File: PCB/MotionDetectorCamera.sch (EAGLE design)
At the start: 186 parts, among them J1 JUMPER-SOLDER, J10 MICROSD-SOCKET, J11 USB-C-JACK, J2 JUMPER-SOLDER, J3 JUMPER-SOLDER, J4 JUMPER-SOLDER, J5 JST-PH-2, J6 JUMPER-SOLDER, J7 JUMPER-SOLDER, J8 JUMPER-SOLDER, J9 S-MOUNT-LENS-HOLDER, Q1 PMOS-NEXPERIA-SOT1220, Q2 PMOS-NEXPERIA-SOT1220, Q3 PMOS-NEXPERIA-SOT1220, U1 TI-TPS2116, U10 TI-TPS22919DCK, U11 TI-TPS62A01, U13 TI-TPS22919DCK, U14 TI-TPS22919DCK, U15 TI-MSP430FR2422IRHL, U16 NXP-NTB0102, U17 NXP-NTB0102, U18 PANASONIC-EKMB110711X, U19 LATTICE-ICE40HX4K-BG121, U2 DIODESINC-AP7350, U20 WINBOND-W25Q40EW, U21 NEXPERIA-74LVC1G98-OR-INV-INP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, U22 NEXPERIA-74LVC1G98-BUFFER, U23 ON-AR0330CS1C12SPKA0, U24 ALLIANCE-AS4C8M16MSA-6BIN, U25 STM-STM32F730, U26 DIODESINC-DT1446-04V-7, U27 NEXPERIA-74LVC1G98-BUFFER, U3 NEXPERIA-74LVC1G98-NOR, U4 MICROCHIP-MCP7383X, U5 EATON-STN101, U6 TI-TPS62A01, U7 TI-TPS62A01, U9 TI-TPS22919DCK, X1 EPSON-FC-135, X2 SITIME-SIT8021, X3 SITIME-SIT8021

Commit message: Switch to smaller lens holder (PT-LH008P)
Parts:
- J9: value S-MOUNT-LENS-HOLDER -> S-MOUNT-LENS-HOLDERM12LENSES-PT-LH008P; device EagleLibrary:S-MOUNT-LENS-HOLDER -> EagleLibrary:S-MOUNT-LENS-HOLDERM12LENSES-PT-LH008P; MFG Marshall Electronics -> (none); PN V-LH4 -> (none)
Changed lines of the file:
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@@
 </part>
 <part name="TP2" library="EagleLibrary" deviceset="TEST-POINT" device=""/>
-<part name="J9" library="EagleLibrary" deviceset="S-MOUNT-LENS-HOLDER" device="">
-<attribute name="MFG" value="Marshall Electronics"/>
-<attribute name="PN" value="V-LH4"/>
-</part>
+<part name="J9" library="EagleLibrary" deviceset="S-MOUNT-LENS-HOLDER" device="M12LENSES-PT-LH008P"/>
 <part name="U25" library="EagleLibrary" deviceset="STM-STM32F730" device="">
 <attribute name="PN" value="STM32F730I8K6"/>

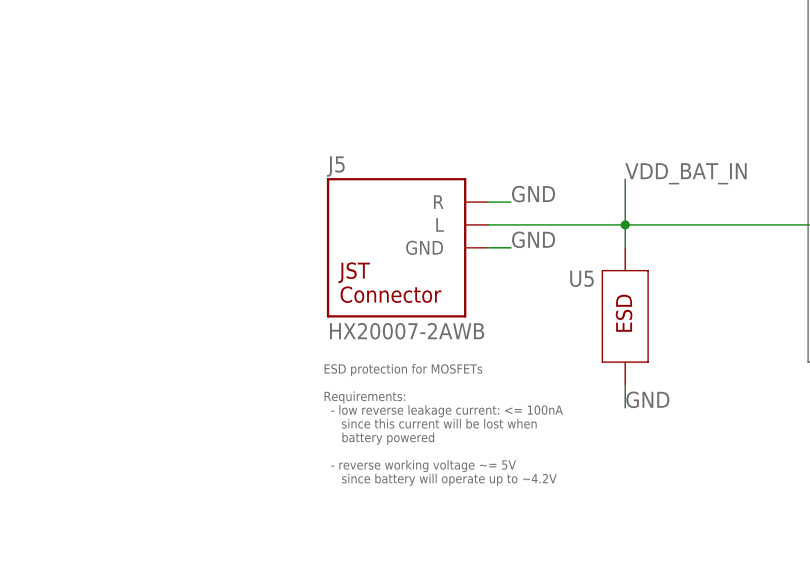
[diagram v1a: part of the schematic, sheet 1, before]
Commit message: Replace battery connector with a smaller version, and move it to the front of the board
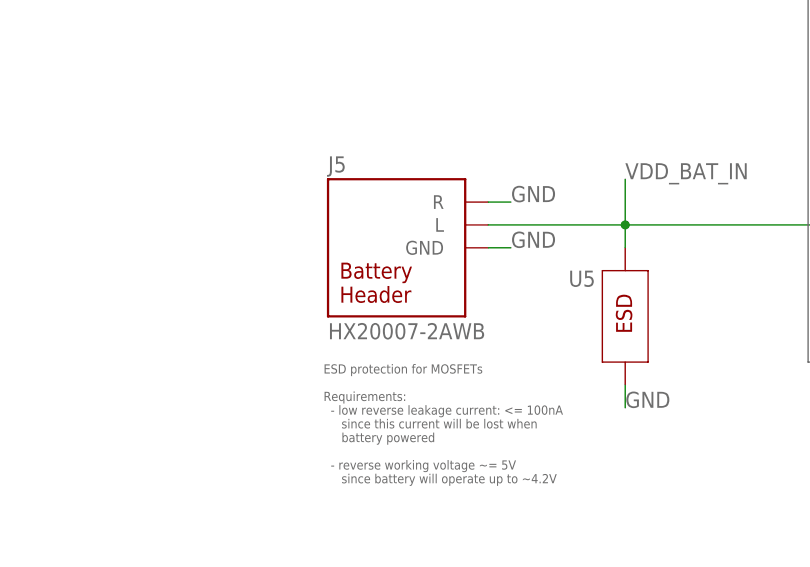
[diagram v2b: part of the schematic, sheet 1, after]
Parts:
- J5: value JST-PH-2 -> JST-SM02B-SRSS-TB; device EagleLibrary:JST-PH-2 -> EagleLibrary:JST-SM02B-SRSS-TB
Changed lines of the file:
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@@
 <attribute name="PN" value="STN101050B101"/>
 </part>
-<part name="J5" library="EagleLibrary" deviceset="JST-PH-2" device="">
+<part name="J5" library="EagleLibrary" deviceset="JST-SM02B-SRSS-TB" device="">
 <attribute name="MFG" value="HX (Zhejiang Yueqing Hongxing Elec)"/>
 <attribute name="MFG2" value="HDGC"/>

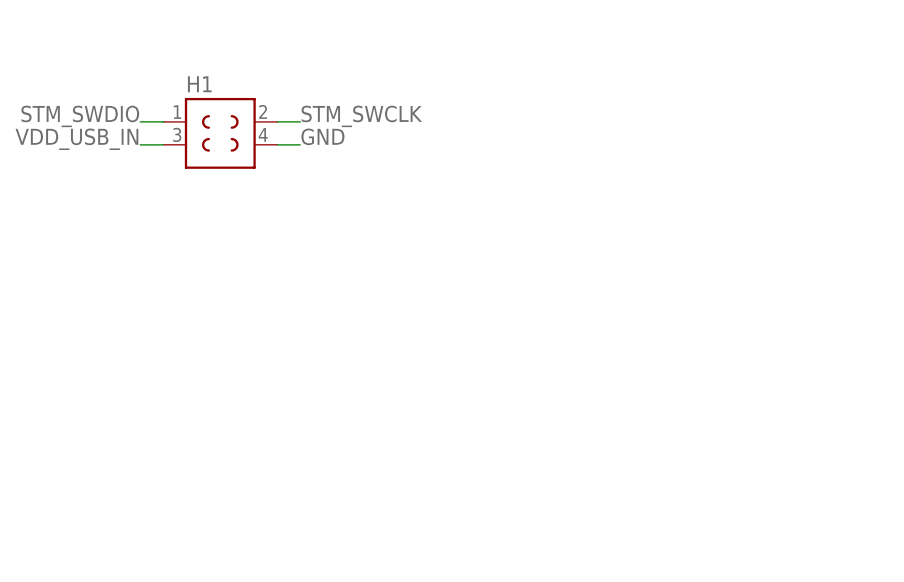
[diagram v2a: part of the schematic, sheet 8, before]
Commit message: Replace STM32 header with 6-pin TagConnect
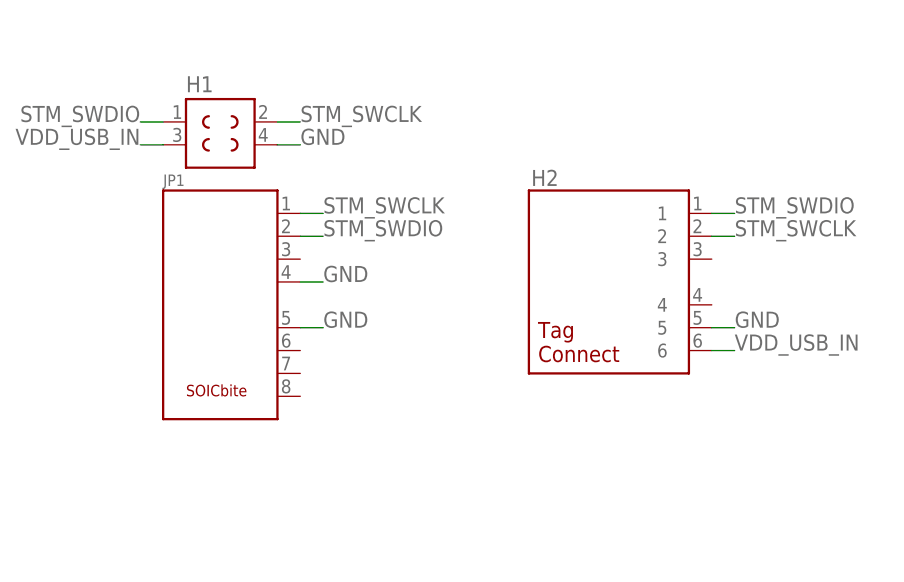
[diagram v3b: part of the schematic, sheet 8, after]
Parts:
- added H2: TAGCONNECT-TC2030-NL, EagleLibrary:TAGCONNECT-TC2030-NL
- added JP1: SOICBITE, EagleLibrary:SOICBITE
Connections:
- net GND: now also H2.5, JP1.P$4, JP1.P$5
- net STM_SWCLK: now also H2.2, JP1.P$1
- net STM_SWDIO: now also H2.1, JP1.P$2
- net VDD_USB_IN: now also H2.6
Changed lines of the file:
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@@
 <attribute name="PN" value="CL21A226MQQNNNG"/>
 </part>
+<part name="JP1" library="EagleLibrary" deviceset="SOICBITE" device=""/>
+<part name="H2" library="EagleLibrary" deviceset="TAGCONNECT-TC2030-NL" device=""/>
 </parts>
 <sheets>
@@
 <attribute name="NAME" x="223.52" y="-83.058" size="1.778" layer="95"/>
 </instance>
+<instance part="JP1" gate="G$1" x="220.98" y="-93.98" smashed="yes">
+<attribute name="NAME" x="220.98" y="-93.472" size="1.27" layer="95"/>
+</instance>
+<instance part="H2" gate="A" x="261.62" y="-93.98" smashed="yes">
+<attribute name="NAME" x="261.874" y="-93.472" size="1.778" layer="95"/>
+</instance>
 </instances>
 <busses>
@@
 <label x="81.28" y="-139.7" size="1.778" layer="95"/>
 </segment>
+<segment>
+<pinref part="JP1" gate="G$1" pin="P$4"/>
+<wire x1="236.22" y1="-104.14" x2="238.76" y2="-104.14" width="0.1524" layer="91"/>
+<label x="238.76" y="-104.14" size="1.778" layer="95"/>
+</segment>
+<segment>
+<pinref part="JP1" gate="G$1" pin="P$5"/>
+<wire x1="236.22" y1="-109.22" x2="238.76" y2="-109.22" width="0.1524" layer="91"/>
+<label x="238.76" y="-109.22" size="1.778" layer="95"/>
+</segment>
+<segment>
+<pinref part="H2" gate="A" pin="5"/>
+<wire x1="281.94" y1="-109.22" x2="284.48" y2="-109.22" width="0.1524" layer="91"/>
+<label x="284.48" y="-109.22" size="1.778" layer="95"/>
+</segment>
 </net>
 <net name="VDD_B_1V8_STM" class="0">
@@
 <pinref part="H1" gate="G$1" pin="1"/>
 </segment>
+<segment>
+<pinref part="JP1" gate="G$1" pin="P$2"/>
+<wire x1="236.22" y1="-99.06" x2="238.76" y2="-99.06" width="0.1524" layer="91"/>
+<label x="238.76" y="-99.06" size="1.778" layer="95"/>
+</segment>
+<segment>
+<pinref part="H2" gate="A" pin="1"/>
+<wire x1="281.94" y1="-96.52" x2="284.48" y2="-96.52" width="0.1524" layer="91"/>
+<label x="284.48" y="-96.52" size="1.778" layer="95"/>
+</segment>
 </net>
 <net name="STM_SWCLK" class="0">
@@
 <pinref part="H1" gate="G$1" pin="2"/>
 </segment>
+<segment>
+<pinref part="JP1" gate="G$1" pin="P$1"/>
+<wire x1="236.22" y1="-96.52" x2="238.76" y2="-96.52" width="0.1524" layer="91"/>
+<label x="238.76" y="-96.52" size="1.778" layer="95"/>
+</segment>
+<segment>
+<pinref part="H2" gate="A" pin="2"/>
+<wire x1="281.94" y1="-99.06" x2="284.48" y2="-99.06" width="0.1524" layer="91"/>
+<label x="284.48" y="-99.06" size="1.778" layer="95"/>
+</segment>
 </net>
 <net name="ICE_STM_SPI_D2" class="0">
@@
 <pinref part="H1" gate="G$1" pin="3"/>
 </segment>
+<segment>
+<pinref part="H2" gate="A" pin="6"/>
+<wire x1="281.94" y1="-111.76" x2="284.48" y2="-111.76" width="0.1524" layer="91"/>
+<label x="284.48" y="-111.76" size="1.778" layer="95"/>
+</segment>
 </net>

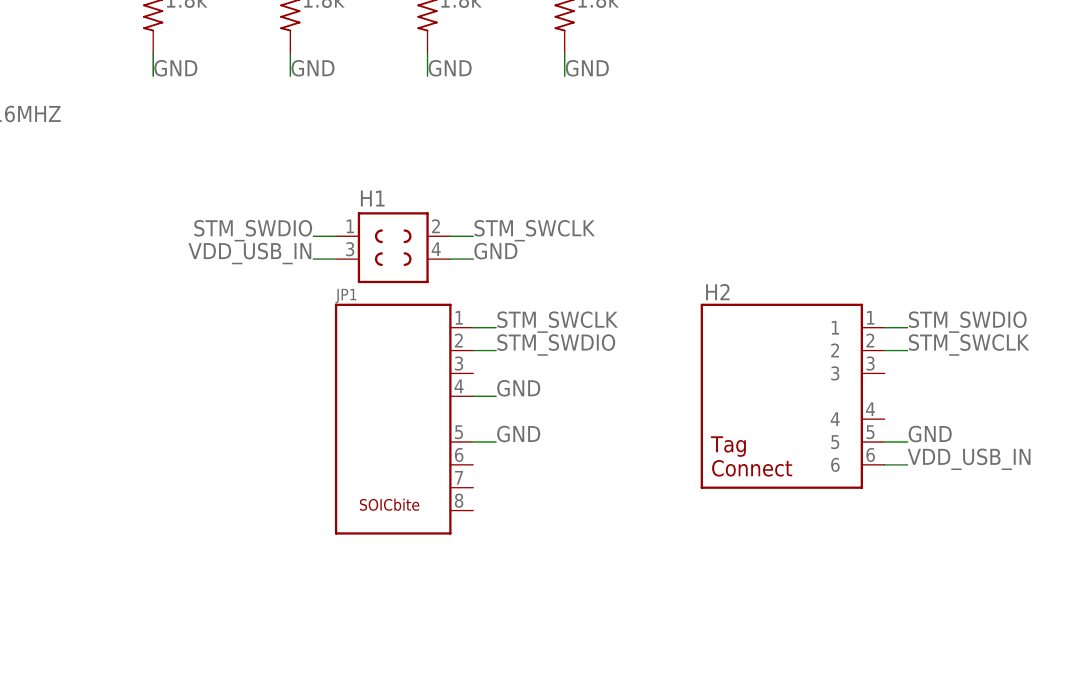
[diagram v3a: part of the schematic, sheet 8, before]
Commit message: Remove old STM32 header
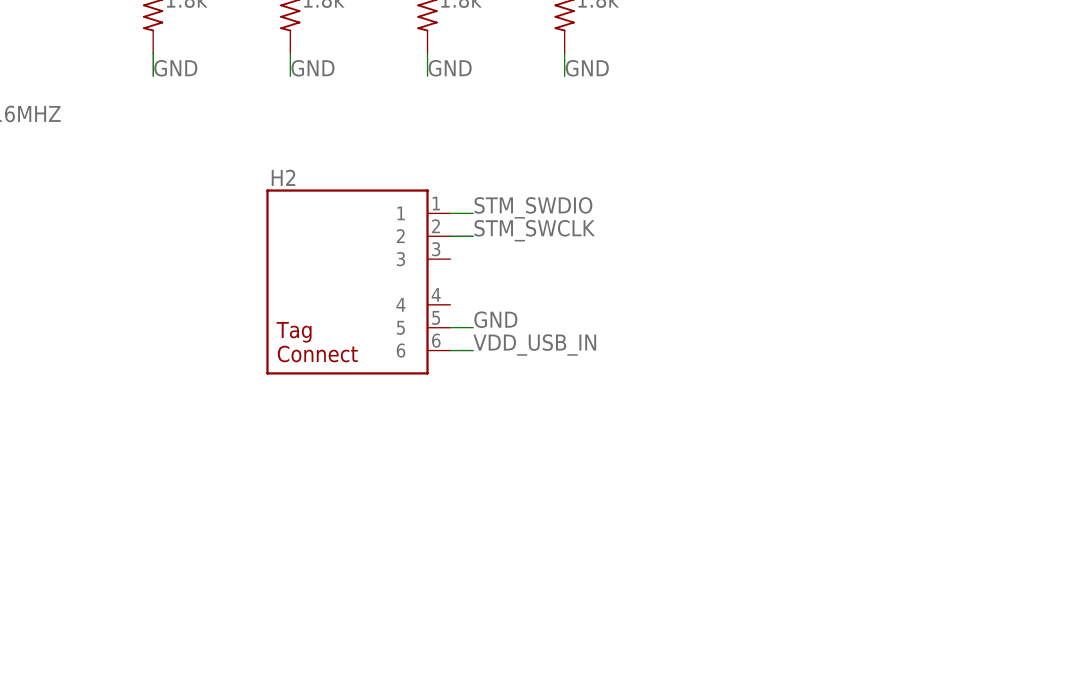
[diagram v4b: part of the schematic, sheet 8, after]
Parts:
- removed H1: HEADER-2X2, EagleLibrary:HEADER-2X2
- removed JP1: SOICBITE, EagleLibrary:SOICBITE
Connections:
- net GND: no longer H1.4, JP1.P$4, JP1.P$5
- net STM_SWCLK: no longer H1.2, JP1.P$1
- net STM_SWDIO: no longer H1.1, JP1.P$2
- net VDD_USB_IN: no longer H1.3
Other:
- moved on the sheet: H2
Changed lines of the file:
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@@
 <attribute name="PN" value="AC0402FR-075K1L"/>
 </part>
-<part name="H1" library="EagleLibrary" deviceset="HEADER-2X2" device=""/>
 <part name="J4" library="EagleLibrary" deviceset="JUMPER" device="-SOLDER" value="JUMPER-SOLDER"/>
 <part name="U27" library="EagleLibrary" deviceset="NEXPERIA-74LVC1G98-BUFFER" device="">
@@
 <attribute name="PN" value="CL21A226MQQNNNG"/>
 </part>
-<part name="JP1" library="EagleLibrary" deviceset="SOICBITE" device=""/>
 <part name="H2" library="EagleLibrary" deviceset="TAGCONNECT-TC2030-NL" device=""/>
 </parts>
@@
 <attribute name="MFG" x="25.4" y="-276.86" size="1.778" layer="96" display="off"/>
 </instance>
-<instance part="H1" gate="G$1" x="223.52" y="-83.82" smashed="yes">
-<attribute name="NAME" x="223.52" y="-83.058" size="1.778" layer="95"/>
-</instance>
-<instance part="JP1" gate="G$1" x="220.98" y="-93.98" smashed="yes">
-<attribute name="NAME" x="220.98" y="-93.472" size="1.27" layer="95"/>
-</instance>
-<instance part="H2" gate="A" x="261.62" y="-93.98" smashed="yes">
-<attribute name="NAME" x="261.874" y="-93.472" size="1.778" layer="95"/>
+<instance part="H2" gate="A" x="213.36" y="-81.28" smashed="yes">
+<attribute name="NAME" x="213.614" y="-80.772" size="1.778" layer="95"/>
 </instance>
 </instances>
@@
 </segment>
 <segment>
-<wire x1="233.68" y1="-88.9" x2="236.22" y2="-88.9" width="0.1524" layer="91"/>
-<label x="236.22" y="-88.9" size="1.778" layer="95"/>
-<pinref part="H1" gate="G$1" pin="4"/>
-</segment>
-<segment>
 <pinref part="U25" gate="J" pin="BOOT0_D6"/>
 <wire x1="78.74" y1="-139.7" x2="81.28" y2="-139.7" width="0.1524" layer="91"/>
@@
 </segment>
 <segment>
-<pinref part="JP1" gate="G$1" pin="P$4"/>
-<wire x1="236.22" y1="-104.14" x2="238.76" y2="-104.14" width="0.1524" layer="91"/>
-<label x="238.76" y="-104.14" size="1.778" layer="95"/>
-</segment>
-<segment>
-<pinref part="JP1" gate="G$1" pin="P$5"/>
-<wire x1="236.22" y1="-109.22" x2="238.76" y2="-109.22" width="0.1524" layer="91"/>
-<label x="238.76" y="-109.22" size="1.778" layer="95"/>
-</segment>
-<segment>
 <pinref part="H2" gate="A" pin="5"/>
-<wire x1="281.94" y1="-109.22" x2="284.48" y2="-109.22" width="0.1524" layer="91"/>
-<label x="284.48" y="-109.22" size="1.778" layer="95"/>
+<wire x1="233.68" y1="-96.52" x2="236.22" y2="-96.52" width="0.1524" layer="91"/>
+<label x="236.22" y="-96.52" size="1.778" layer="95"/>
 </segment>
 </net>
@@
 </segment>
 <segment>
-<wire x1="220.98" y1="-86.36" x2="218.44" y2="-86.36" width="0.1524" layer="91"/>
-<label x="218.44" y="-86.36" size="1.778" layer="95" align="bottom-right"/>
-<pinref part="H1" gate="G$1" pin="1"/>
-</segment>
-<segment>
-<pinref part="JP1" gate="G$1" pin="P$2"/>
-<wire x1="236.22" y1="-99.06" x2="238.76" y2="-99.06" width="0.1524" layer="91"/>
-<label x="238.76" y="-99.06" size="1.778" layer="95"/>
-</segment>
-<segment>
 <pinref part="H2" gate="A" pin="1"/>
-<wire x1="281.94" y1="-96.52" x2="284.48" y2="-96.52" width="0.1524" layer="91"/>
-<label x="284.48" y="-96.52" size="1.778" layer="95"/>
+<wire x1="233.68" y1="-83.82" x2="236.22" y2="-83.82" width="0.1524" layer="91"/>
+<label x="236.22" y="-83.82" size="1.778" layer="95"/>
 </segment>
 </net>
@@
 </segment>
 <segment>
+<pinref part="H2" gate="A" pin="2"/>
 <wire x1="233.68" y1="-86.36" x2="236.22" y2="-86.36" width="0.1524" layer="91"/>
 <label x="236.22" y="-86.36" size="1.778" layer="95"/>
-<pinref part="H1" gate="G$1" pin="2"/>
-</segment>
-<segment>
-<pinref part="JP1" gate="G$1" pin="P$1"/>
-<wire x1="236.22" y1="-96.52" x2="238.76" y2="-96.52" width="0.1524" layer="91"/>
-<label x="238.76" y="-96.52" size="1.778" layer="95"/>
-</segment>
-<segment>
-<pinref part="H2" gate="A" pin="2"/>
-<wire x1="281.94" y1="-99.06" x2="284.48" y2="-99.06" width="0.1524" layer="91"/>
-<label x="284.48" y="-99.06" size="1.778" layer="95"/>
 </segment>
 </net>
@@
 <net name="VDD_USB_IN" class="0">
 <segment>
-<wire x1="220.98" y1="-88.9" x2="218.44" y2="-88.9" width="0.1524" layer="91"/>
-<label x="218.44" y="-88.9" size="1.778" layer="95" align="bottom-right"/>
-<pinref part="H1" gate="G$1" pin="3"/>
-</segment>
-<segment>
 <pinref part="H2" gate="A" pin="6"/>
-<wire x1="281.94" y1="-111.76" x2="284.48" y2="-111.76" width="0.1524" layer="91"/>
-<label x="284.48" y="-111.76" size="1.778" layer="95"/>
+<wire x1="233.68" y1="-99.06" x2="236.22" y2="-99.06" width="0.1524" layer="91"/>
+<label x="236.22" y="-99.06" size="1.778" layer="95"/>
 </segment>
 </net>

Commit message: Layout progress
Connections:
- net STM_SWCLK: now also H2.4; no longer H2.2
- net STM_SWDIO: now also H2.6; no longer H2.1
- net VDD_USB_IN: now also H2.1; no longer H2.6
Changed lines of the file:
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@@
+</segment>
+<segment>
+<wire x1="256.54" y1="-96.52" x2="259.08" y2="-96.52" width="0.1524" layer="91"/>
+<label x="259.08" y="-96.52" size="1.778" layer="95"/>
 </segment>
 <segment>
@@
 </segment>
 <segment>
-<pinref part="H2" gate="A" pin="1"/>
-<wire x1="233.68" y1="-83.82" x2="236.22" y2="-83.82" width="0.1524" layer="91"/>
-<label x="236.22" y="-83.82" size="1.778" layer="95"/>
+<wire x1="256.54" y1="-83.82" x2="259.08" y2="-83.82" width="0.1524" layer="91"/>
+<label x="259.08" y="-83.82" size="1.778" layer="95"/>
+</segment>
+<segment>
+<pinref part="H2" gate="A" pin="6"/>
+<wire x1="233.68" y1="-99.06" x2="236.22" y2="-99.06" width="0.1524" layer="91"/>
+<label x="236.22" y="-99.06" size="1.778" layer="95"/>
 </segment>
 </net>
@@
 </segment>
 <segment>
-<pinref part="H2" gate="A" pin="2"/>
-<wire x1="233.68" y1="-86.36" x2="236.22" y2="-86.36" width="0.1524" layer="91"/>
-<label x="236.22" y="-86.36" size="1.778" layer="95"/>
+<wire x1="256.54" y1="-86.36" x2="259.08" y2="-86.36" width="0.1524" layer="91"/>
+<label x="259.08" y="-86.36" size="1.778" layer="95"/>
+</segment>
+<segment>
+<pinref part="H2" gate="A" pin="4"/>
+<wire x1="233.68" y1="-93.98" x2="236.22" y2="-93.98" width="0.1524" layer="91"/>
+<label x="236.22" y="-93.98" size="1.778" layer="95"/>
 </segment>
 </net>
@@
 </segment>
 </net>
-<net name="VDD_USB_IN" class="0">
-<segment>
-<pinref part="H2" gate="A" pin="6"/>
-<wire x1="233.68" y1="-99.06" x2="236.22" y2="-99.06" width="0.1524" layer="91"/>
-<label x="236.22" y="-99.06" size="1.778" layer="95"/>
-</segment>
-</net>
 <net name="N$29" class="0">
 <segment>
@@
 </segment>
 </net>
+<net name="VDD_USB_IN" class="0">
+<segment>
+<wire x1="256.54" y1="-99.06" x2="259.08" y2="-99.06" width="0.1524" layer="91"/>
+<label x="259.08" y="-99.06" size="1.778" layer="95"/>
+</segment>
+<segment>
+<pinref part="H2" gate="A" pin="1"/>
+<wire x1="233.68" y1="-83.82" x2="236.22" y2="-83.82" width="0.1524" layer="91"/>
+<label x="236.22" y="-83.82" size="1.778" layer="95"/>
+</segment>
+</net>
